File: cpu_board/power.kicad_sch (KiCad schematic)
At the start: 29 parts, among them U8 TPS54226PWPRPWP14_2P31X2P46-L, U9 TPS54226PWPRPWP14_2P31X2P46-L

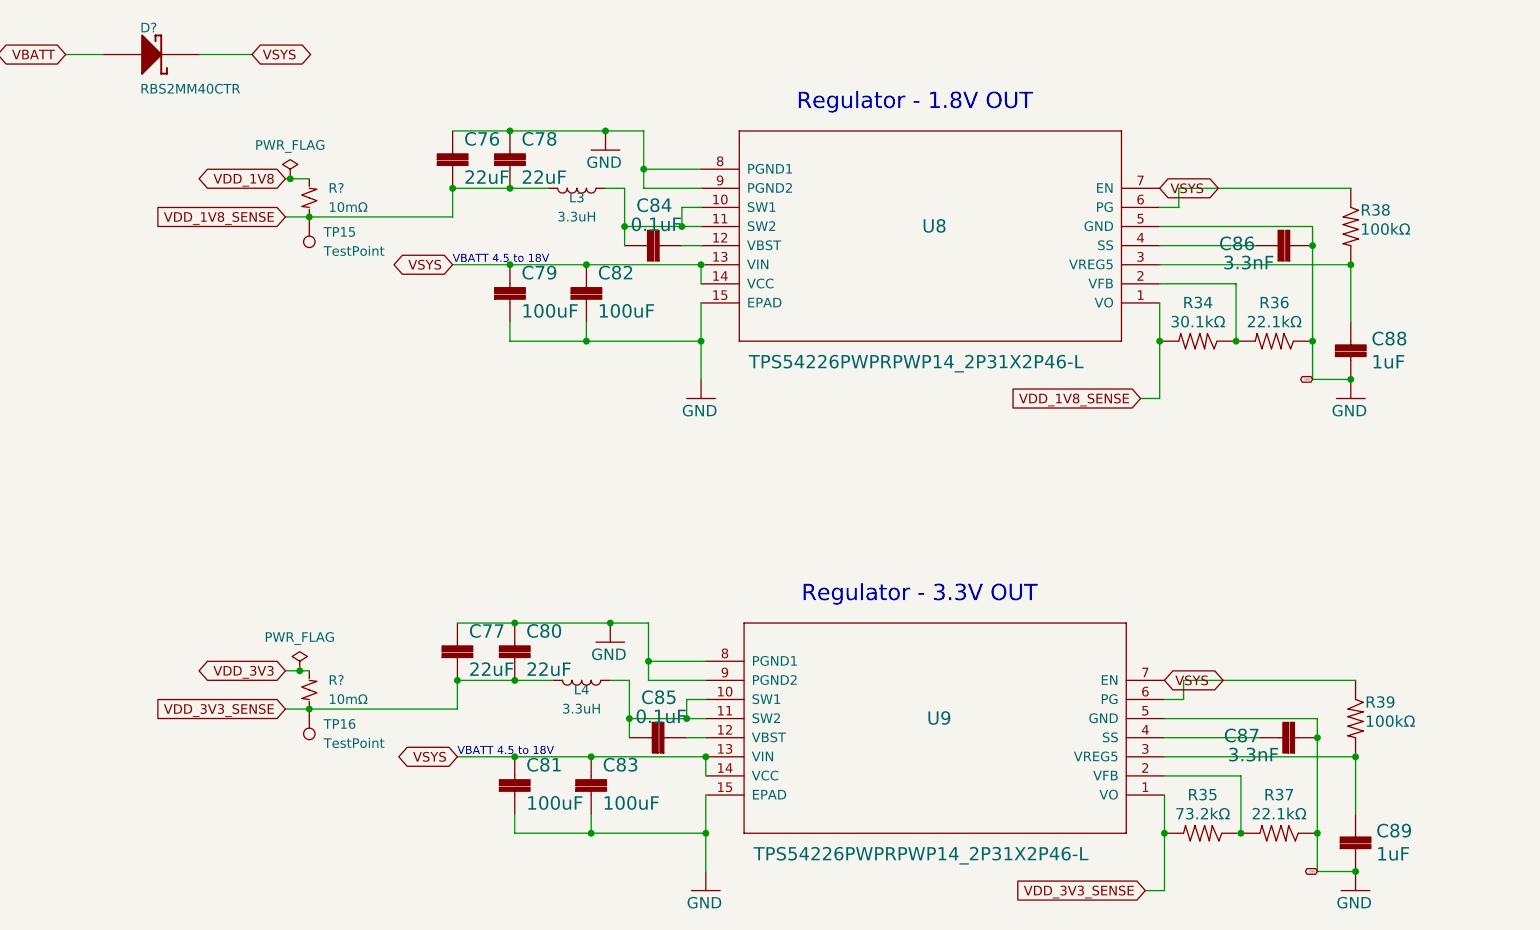
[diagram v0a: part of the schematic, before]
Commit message: route most of power distribution
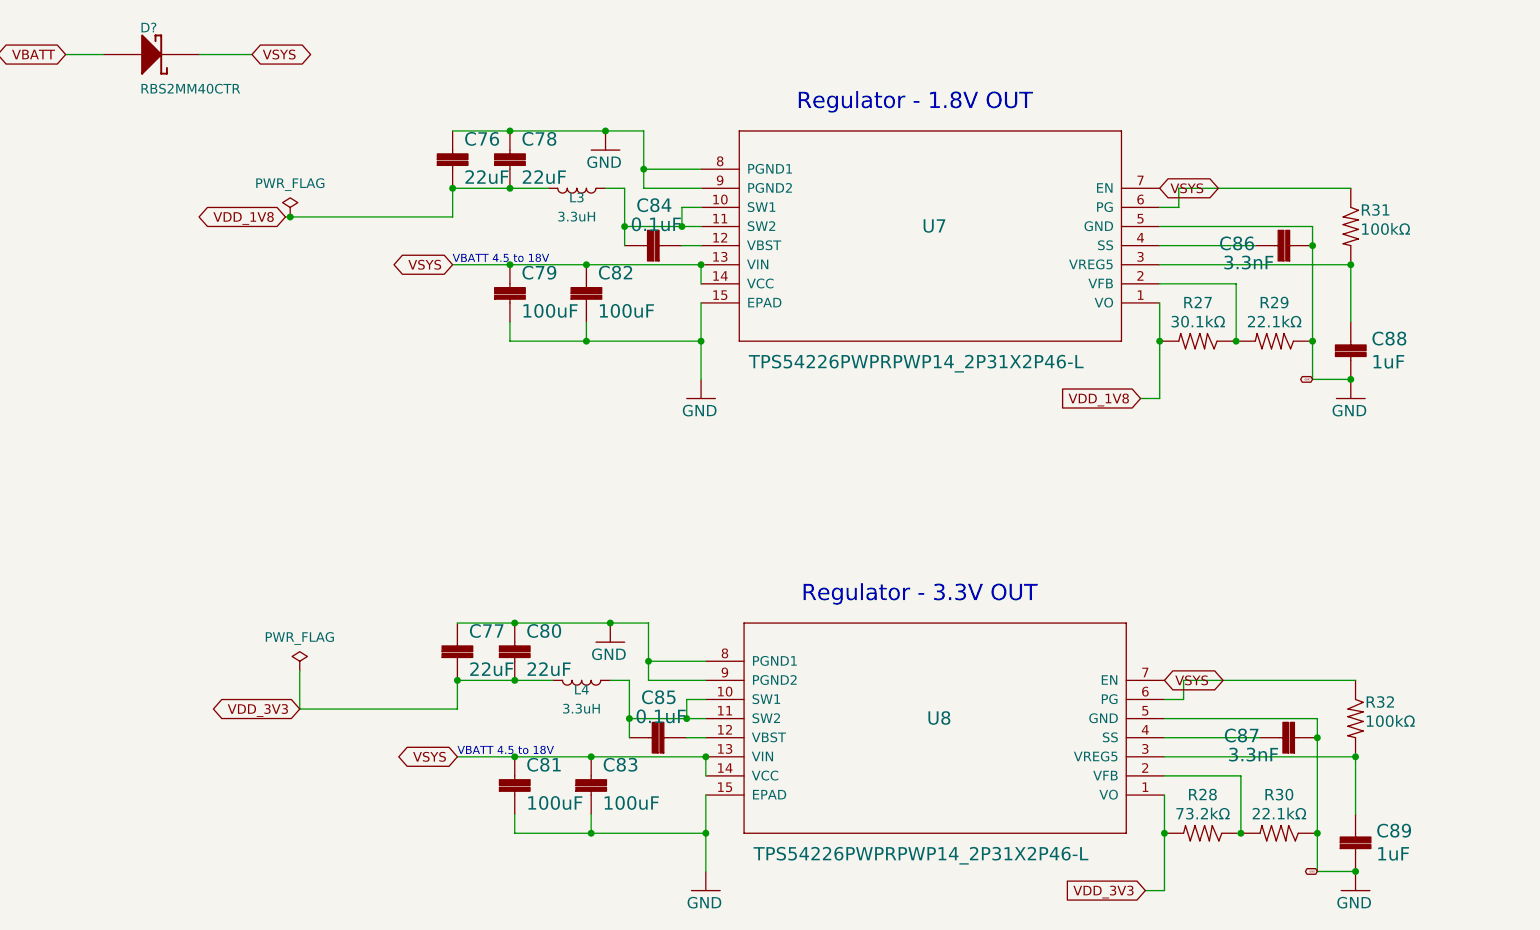
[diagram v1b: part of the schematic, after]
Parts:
- removed R? (x2): 10mΩ, Resistor_SMD:R_0603_1608Metric, symbol Device:R_Small_US
- removed TP15, TP16: TestPoint, TestPoint:TestPoint_Pad_1.5x1.5mm, symbol Connector:TestPoint
- renumbered R34 to R27, R35 to R28, R36 to R29, R37 to R30, R38 to R31, R39 to R32, U8 to U7, U9 to U8
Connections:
- net VDD_1V8_SENSE is gone; now on net VDD_1V8: C76.2, C78.2, L3.2, R27.2, U7.1 (VO)
- net VDD_3V3_SENSE is gone; now on net VDD_3V3: C77.2, C80.2, L4.2, R28.2, U8.1 (VO)

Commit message: continue work on fanout
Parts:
- C76, C77, C78, C80, C84, C85, C86, C87, C88, C89: footprint Capacitor_SMD:C_0402_1005Metric -> adcs:Perfect_0402
- C79, C81, C82, C83: footprint Capacitor_SMD:C_1210_3225Metric -> adcs:Perfect_0402
- R27, R28, R29, R30, R31, R32: footprint Resistor_SMD:R_0402_1005Metric -> adcs:Perfect_0402
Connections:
- net VSYS: no longer U7.7 (EN), U8.7 (EN)
- new net PMIC_ON_REQ: U7.7 (EN), U8.7 (EN)
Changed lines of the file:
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@@
+    (stroke (width 0) (type default))
+  )
+  (wire (pts (xy 247.015 104.14) (xy 247.015 109.22))
     (stroke (width 0) (type default))
   )
@@
   )
   (wire (pts (xy 247.015 124.46) (xy 247.015 129.54))
+    (stroke (width 0) (type default))
+  )
+  (wire (pts (xy 247.65 168.275) (xy 247.65 174.625))
     (stroke (width 0) (type default))
   )
@@
     (at 159.385 75.565 0)
     (effects (font (size 1.27 1.27) (color 194 0 0 1)) (justify left bottom))
+  )
+  (global_label "PMIC_ON_REQ" (shape bidirectional) (at 247.015 104.14 0) (fields_autoplaced)
+    (effects (font (size 1.27 1.27)) (justify left))
+    (property "Intersheetrefs" "${INTERSHEET_REFS}" (at 264.0534 104.14 0)
+      (effects (font (size 1.27 1.27)) (justify left) hide)
+    )
   )
   (global_label "VSYS" (shape bidirectional) (at 153.035 119.38 180) (fields_autoplaced)
@@
     )
   )
-  (global_label "VSYS" (shape bidirectional) (at 247.65 174.625 0) (fields_autoplaced)
+  (global_label "PMIC_ON_REQ" (shape bidirectional) (at 247.65 168.275 0) (fields_autoplaced)
     (effects (font (size 1.27 1.27)) (justify left))
-    (property "Intersheetrefs" "${INTERSHEET_REFS}" (at 256.3427 174.625 0)
+    (property "Intersheetrefs" "${INTERSHEET_REFS}" (at 264.6884 168.275 0)
       (effects (font (size 1.27 1.27)) (justify left) hide)
     )
@@
     )
   )
-  (global_label "VSYS" (shape bidirectional) (at 247.015 109.22 0) (fields_autoplaced)
-    (effects (font (size 1.27 1.27)) (justify left))
-    (property "Intersheetrefs" "${INTERSHEET_REFS}" (at 255.7077 109.22 0)
-      (effects (font (size 1.27 1.27)) (justify left) hide)
-    )
-  )
   (global_label "VDD_1V8" (shape input) (at 244.475 137.16 180) (fields_autoplaced)
     (effects (font (size 1.27 1.27)) (justify right))
@@
       (effects (font (size 1.778 1.778)) (justify left bottom))
     )
-    (property "Footprint" "Capacitor_SMD:C_0402_1005Metric" (at 180.975 116.84 0)
+    (property "Footprint" "adcs:Perfect_0402" (at 180.975 116.84 0)
       (effects (font (size 1.27 1.27)) hide)
     )
@@
     (property "Footprint (for JLCPCB)" "0402" (at 180.975 116.84 0)
       (effects (font (size 1.27 1.27)) hide)
+    )
+    (property "DigiKey Part Number" "" (at 180.975 116.84 0)
+      (effects (font (size 1.27 1.27)) hide)
+    )
+    (property "Tolerance" "" (at 180.975 116.84 0)
+      (effects (font (size 1.27 1.27)))
+    )
+    (property "Power Rating" "" (at 180.975 116.84 0)
+      (effects (font (size 1.27 1.27)))
     )
     (pin "1")
@@
       (effects (font (size 1.778 1.778)) (justify left))
     )
-    (property "Footprint" "Capacitor_SMD:C_0402_1005Metric" (at 273.05 197.485 0)
+    (property "Footprint" "adcs:Perfect_0402" (at 273.05 197.485 0)
       (effects (font (size 1.27 1.27)) hide)
     )
@@
     (property "Footprint (for JLCPCB)" "0402" (at 273.05 197.485 0)
       (effects (font (size 1.27 1.27)) hide)
+    )
+    (property "DigiKey Part Number" "" (at 273.05 197.485 0)
+      (effects (font (size 1.27 1.27)) hide)
+    )
+    (property "Tolerance" "" (at 273.05 197.485 0)
+      (effects (font (size 1.27 1.27)))
+    )
+    (property "Power Rating" "" (at 273.05 197.485 0)
+      (effects (font (size 1.27 1.27)))
     )
     (pin "1")
@@
       (effects (font (size 1.778 1.778)) (justify left bottom))
     )
-    (property "Footprint" "Capacitor_SMD:C_1210_3225Metric" (at 171.45 189.865 0)
+    (property "Footprint" "adcs:Perfect_0402" (at 171.45 189.865 0)
       (effects (font (size 1.27 1.27)) hide)
     )
@@
       (effects (font (size 1.4986 1.4986)))
     )
-    (property "Footprint" "Resistor_SMD:R_0402_1005Metric" (at 262.89 194.945 0)
+    (property "Footprint" "adcs:Perfect_0402" (at 262.89 194.945 0)
       (effects (font (size 1.27 1.27)) hide)
     )
@@
       (effects (font (size 1.4986 1.4986)))
     )
-    (property "Footprint" "Resistor_SMD:R_0402_1005Metric" (at 252.095 129.54 0)
+    (property "Footprint" "adcs:Perfect_0402" (at 252.095 129.54 0)
       (effects (font (size 1.27 1.27)) hide)
     )
@@
       (effects (font (size 1.4986 1.4986)) (justify left bottom))
     )
-    (property "Footprint" "Resistor_SMD:R_0402_1005Metric" (at 273.05 179.705 0)
+    (property "Footprint" "adcs:Perfect_0402" (at 273.05 179.705 0)
       (effects (font (size 1.27 1.27)) hide)
     )
@@
       (effects (font (size 1.778 1.778)) (justify left bottom))
     )
-    (property "Footprint" "Capacitor_SMD:C_0402_1005Metric" (at 153.035 106.68 0)
+    (property "Footprint" "adcs:Perfect_0402" (at 153.035 106.68 0)
       (effects (font (size 1.27 1.27)) hide)
     )
@@
       (effects (font (size 1.778 1.778)) (justify left bottom))
     )
-    (property "Footprint" "Capacitor_SMD:C_0402_1005Metric" (at 265.43 182.245 0)
+    (property "Footprint" "adcs:Perfect_0402" (at 265.43 182.245 0)
       (effects (font (size 1.27 1.27)) hide)
     )
@@
     (property "Footprint (for JLCPCB)" "0402" (at 265.43 182.245 0)
       (effects (font (size 1.27 1.27)) hide)
+    )
+    (property "DigiKey Part Number" "" (at 265.43 182.245 0)
+      (effects (font (size 1.27 1.27)) hide)
+    )
+    (property "Tolerance" "" (at 265.43 182.245 0)
+      (effects (font (size 1.27 1.27)))
+    )
+    (property "Power Rating" "" (at 265.43 182.245 0)
+      (effects (font (size 1.27 1.27)))
     )
     (pin "1")
@@
       (effects (font (size 1.778 1.778)) (justify left))
     )
-    (property "Footprint" "Capacitor_SMD:C_0402_1005Metric" (at 272.415 132.08 0)
+    (property "Footprint" "adcs:Perfect_0402" (at 272.415 132.08 0)
       (effects (font (size 1.27 1.27)) hide)
     )
@@
       (effects (font (size 1.27 1.27)) hide)
     )
+    (property "DigiKey Part Number" "" (at 272.415 132.08 0)
+      (effects (font (size 1.27 1.27)) hide)
+    )
+    (property "Tolerance" "" (at 272.415 132.08 0)
+      (effects (font (size 1.27 1.27)))
+    )
+    (property "Power Rating" "" (at 272.415 132.08 0)
+      (effects (font (size 1.27 1.27)))
+    )
     (pin "1")
     (pin "2")
@@
       (effects (font (size 1.778 1.778)) (justify left bottom))
     )
-    (property "Footprint" "Capacitor_SMD:C_0402_1005Metric" (at 264.795 116.84 0)
+    (property "Footprint" "adcs:Perfect_0402" (at 264.795 116.84 0)
       (effects (font (size 1.27 1.27)) hide)
     )
@@
       (effects (font (size 1.27 1.27)) hide)
     )
+    (property "DigiKey Part Number" "" (at 264.795 116.84 0)
+      (effects (font (size 1.27 1.27)) hide)
+    )
+    (property "Tolerance" "" (at 264.795 116.84 0)
+      (effects (font (size 1.27 1.27)))
+    )
+    (property "Power Rating" "" (at 264.795 116.84 0)
+      (effects (font (size 1.27 1.27)))
+    )
     (pin "1")
     (pin "2")
@@
       (effects (font (size 1.778 1.778)) (justify left bottom))
     )
-    (property "Footprint" "Capacitor_SMD:C_1210_3225Metric" (at 170.815 124.46 0)
+    (property "Footprint" "adcs:Perfect_0402" (at 170.815 124.46 0)
       (effects (font (size 1.27 1.27)) hide)
     )
@@
       (effects (font (size 1.4986 1.4986)))
     )
-    (property "Footprint" "Resistor_SMD:R_0402_1005Metric" (at 252.73 194.945 0)
+    (property "Footprint" "adcs:Perfect_0402" (at 252.73 194.945 0)
       (effects (font (size 1.27 1.27)) hide)
     )
@@
       (effects (font (size 1.4986 1.4986)))
     )
-    (property "Footprint" "Resistor_SMD:R_0402_1005Metric" (at 262.255 129.54 0)
+    (property "Footprint" "adcs:Perfect_0402" (at 262.255 129.54 0)
       (effects (font (size 1.27 1.27)) hide)
     )
@@
       (effects (font (size 1.778 1.778)) (justify left bottom))
     )
-    (property "Footprint" "Capacitor_SMD:C_0402_1005Metric" (at 153.67 172.085 0)
+    (property "Footprint" "adcs:Perfect_0402" (at 153.67 172.085 0)
       (effects (font (size 1.27 1.27)) hide)
     )
@@
       (effects (font (size 1.778 1.778)) (justify left bottom))
     )
-    (property "Footprint" "Capacitor_SMD:C_0402_1005Metric" (at 160.655 106.68 0)
+    (property "Footprint" "adcs:Perfect_0402" (at 160.655 106.68 0)
       (effects (font (size 1.27 1.27)) hide)
     )
@@
       (effects (font (size 1.778 1.778)) (justify left bottom))
     )
-    (property "Footprint" "Capacitor_SMD:C_0402_1005Metric" (at 161.29 172.085 0)
+    (property "Footprint" "adcs:Perfect_0402" (at 161.29 172.085 0)
       (effects (font (size 1.27 1.27)) hide)
     )
@@
       (effects (font (size 1.4986 1.4986)) (justify left bottom))
     )
-    (property "Footprint" "Resistor_SMD:R_0402_1005Metric" (at 272.415 114.3 0)
+    (property "Footprint" "adcs:Perfect_0402" (at 272.415 114.3 0)
       (effects (font (size 1.27 1.27)) hide)
     )
@@
       (effects (font (size 1.778 1.778)) (justify left bottom))
     )
-    (property "Footprint" "Capacitor_SMD:C_1210_3225Metric" (at 161.29 189.865 0)
+    (property "Footprint" "adcs:Perfect_0402" (at 161.29 189.865 0)
       (effects (font (size 1.27 1.27)) hide)
     )
@@
       (effects (font (size 1.778 1.778)) (justify left bottom))
     )
-    (property "Footprint" "Capacitor_SMD:C_0402_1005Metric" (at 181.61 182.245 0)
+    (property "Footprint" "adcs:Perfect_0402" (at 181.61 182.245 0)
       (effects (font (size 1.27 1.27)) hide)
     )
@@
     (property "Footprint (for JLCPCB)" "0402" (at 181.61 182.245 0)
       (effects (font (size 1.27 1.27)) hide)
+    )
+    (property "DigiKey Part Number" "" (at 181.61 182.245 0)
+      (effects (font (size 1.27 1.27)) hide)
+    )
+    (property "Tolerance" "" (at 181.61 182.245 0)
+      (effects (font (size 1.27 1.27)))
+    )
+    (property "Power Rating" "" (at 181.61 182.245 0)
+      (effects (font (size 1.27 1.27)))
     )
     (pin "1")
@@
       (effects (font (size 1.778 1.778)) (justify left bottom))
     )
-    (property "Footprint" "Capacitor_SMD:C_1210_3225Metric" (at 160.655 124.46 0)
-      (effects (font (size 1.27 1.27)) hide)
-    )
+    (property "Footprint" "adcs:Perfect_0402" (at 160.655 124.46 0)
+      (effects (font (size 1.27 1.27)) hide)
+    )

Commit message: add load switch
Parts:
- removed D?: RBS2MM40CTR, adcs:SOD123_AK, symbol 04 MAIN POWER-SchDoc-rescue:__Template_DIODE_SCHOTTKY-
- added C16, C7: 100uF, adcs:Perfect_0402, symbol mainboard:22UF-1210-16V-20%
- added C24, C27: 22uF, adcs:Perfect_0402, symbol mainboard:22UF-0805-6.3V-20%
- added C? (x2): 1uF, adcs:Perfect_0402, symbol Device:C_Small
- added C?: 22nF, adcs:Perfect_0402, symbol Device:C_Small
- added L?: 330uH, adcs:IND_SRN6045TA-331K, symbol Device:L
- added R5: 18kΩ, adcs:Perfect_0402, symbol Device:R_Small_US
- added R5: 30kΩ, adcs:Perfect_0402, symbol Device:R_Small_US
- added R5: 800kΩ, adcs:Perfect_0402, symbol Device:R_Small_US
- added R5: 2.2MΩ, adcs:Perfect_0402, symbol Device:R_Small_US
- added R5: 10kΩ, adcs:Perfect_0402, symbol Device:R_Small_US
- added R5: 0Ω, adcs:Perfect_0402, symbol Device:R_Small_US
- added R6 (x2): 100kΩ, adcs:Perfect_0402, symbol Device:R_Small_US
- added R6: 1.27MΩ, adcs:Perfect_0402, symbol Device:R_Small_US
- added R?: 10mΩ, Resistor_SMD:R_2512_6332Metric, symbol Device:R_Small_US
- added U1: TPS16630PWPR, HTSSOP20_PWP_TEX, symbol adcs:TPS16630PWPR
- added U10: CD40109BQNSRQ1, NS16, symbol adcs:CD40109BQNSRQ1
- added U9: LT3014IS5-TRMPBF, adcs:S_5_ADI, symbol adcs:LT3014IS5-TRMPBF
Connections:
- net GND: now also C16.2, C24.2, C27.2, C7.2, C?.1, C?.1, C?.1, R5.1, R5.1, R6.1, R6.1, U1.21 (GND), U1.9 (GND), U10.15 (ENABLED), U10.7 (ENABLEB), U10.8 (VSS), U10.9 (ENABLEC), U9.2 (GND)
- net PMIC_ON_REQ: now also U10.3 (A); no longer U7.7 (EN), U8.7 (EN)
- net VBATT: now also C24.1, C27.1, C?.2, L?.2, R5.2, U1.1 (IN), U1.2 (IN), U1.3 (IN), U1.6 (P_IN), U9.1 (IN)
- net VSYS: now also U7.7 (EN), U8.7 (EN), C16.1, C7.1, R5.2, U1.18 (OUT), U1.19 (OUT), U1.20 (OUT)
- new net: R5.2, U1.11 (ILIM)
- new net: R5.2, U1.14 (IMON)
- new net: L?.1, R?.2
- new net: R6.1, R6.2, U1.8 (OVP)
- new net: R5.1, R6.2, U1.7 (UVLO)
- new net: C?.2, U1.10 (DVDT)
- new net: R5.1, R6.2, U9.4 (ADJ)
- new net: R5.2, U1.12 (MODE)
- new net: R5.1, U1.15 (*FLT)
- new net EN_ADCS: U1.13 (*SHDN), U10.4 (E)
- new net EN_LP: U9.3 (*SHDN)
- new net P_GOOD: U1.16 (PGOOD)
- new net VBATT_IN: R?.1
- new net VDD_3V3_LP: C?.2, R5.2, U10.16 (VDD), U9.5 (OUT)
- new net VDD_SNVS_ANA: U10.1 (VCC), U10.2 (ENABLEA)
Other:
- note added: "1.22 * (1 + 2.2 / 1.27) + 0.000004 * 2.2 = 3.33V"
- note added: "Could also use EN_ADCS here, in case the E-fuse shorts on"
- note added: "Do I need a PMIC? In my read of datasheet, PMIC on req and PMIC standby req are just outputs of the RT1176 What should I do with the enables on my regulators? - I think most effective debugging would be to have a way to power cycle the whole board. But if we do that while the wheels are spinning, we will mess stuff up - EDIT: decided to put most of the CPU (and eventual peripherals) on a load swi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"
- note added: "ILim = 1A"
- note added: "Level Shifter"
- note added: "Level shift PMIC_ON_REQ from 1.8V to 3.3V for the Load Switch Qualified by ESA, page 64 Issue 246"
- note added: "Load Switch"
- note added: "PGOOD is high if power supply is on"
- note added: "Solder bridge R1, DNP R2, R3 for default settings"
- note added: "To enable the device, SHDN must be pulled up to at least 2 V."
- note added: "V(OVPR) = 1.2 V and V(UVLOR) = 1.2 V V_OV = 12V V_UV = 6V Set R2 = 100k, solve eq. 8 in datasheet for R1 + R2 = 900k Solve eq 9. to find R3 = 100k, and compute R1 = 800k"
- note added: "set voltage"
- note removed: "Do I need a PMIC? In my read of datasheet, PMIC on req and PMIC standby req are just outputs of the RT1176 What should I do with the enables on my regulators? - I think most effective debugging would be to have a way to power cycle the whole board. But if we do that while the wheels are spinning, we will mess stuff up"
- moved on the sheet: C76, C77, C78, C79, C80, C81, C82, C83, C84, C85, C86, C87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
